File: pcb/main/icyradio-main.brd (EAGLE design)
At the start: 167.7 x 111.2 mm, 700 parts, among them CON101 FPC-22P, CON102 FPC-22P, CON1101 2EDG-2P-5MM-H, CON701 4P-SH-TOP, CON801 PCIE-X4-EDGE, J101 RJ45_MAG_LED_1G-TE-1-2301994-0, J701 TRSJACK, J702 TRSJACK, J703 TRSJACK, M701 SPH0641LM4H-1, M702 SPH0641LM4H-1, Q101 AO3400, Q102 AO3400, Q1101 AO3400, Q1102 AO4805, Q1103 AO3400, Q1104 AO4805, Q1105 AO4805, Q1106 AO3400, T501 UWB1-85E, T502 UWB1-85E, T503 UWB1-85E, T504 UWB1-85E, T505 UWB1-85E, T506 UWB1-85E, T507 UWB1-85E, T508 UWB1-85E, U1001 LTC4313-3, U1002 UPD301C, U1003 MIC2019, U101 MIC2019, U102 RPI-CM4, U1101 MCP1804-3302, U1102 LT7182S, U1201 ADM7172ACPZ-5.0, U1202 ADM7171ACPZ-1.3, U1203 ADM7171ACPZ-3.3, U1204 MIC23159, U1205 MIC5166, U1206 ADM7171ACPZ-1.3, U1207 ADM7171ACPZ-3.3, U1208 MIC23159, U1209 MIC23155, U1210 ADP7142AUJZ-3.3, U201 XC7A100TFGG484, U202 SST26VF064B, U301 MT41K256M16TW-125, U401 AD9361, U501 MIC2019, U502 MIC2019, U503 MIC2019, U504 MIC2019, U505 ADL5601, U506 ADL5601, U601 8V97003, U701 ADAU1372, U901 DSB321SDA, U902 SI5351C-B-GM

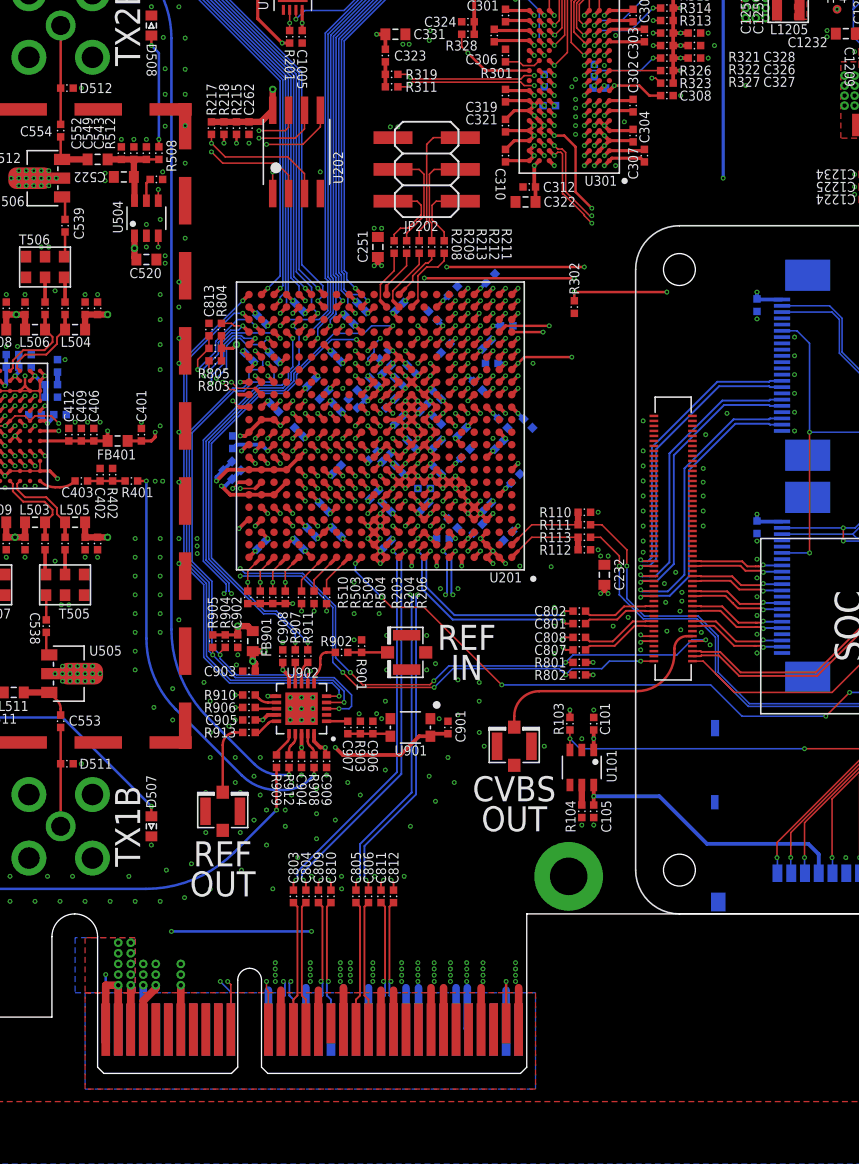
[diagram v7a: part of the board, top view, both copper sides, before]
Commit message: Some PCB rectifications and removal of old gerbers
Signed-off-by: João Silva <jgc3silva@gmail.com>
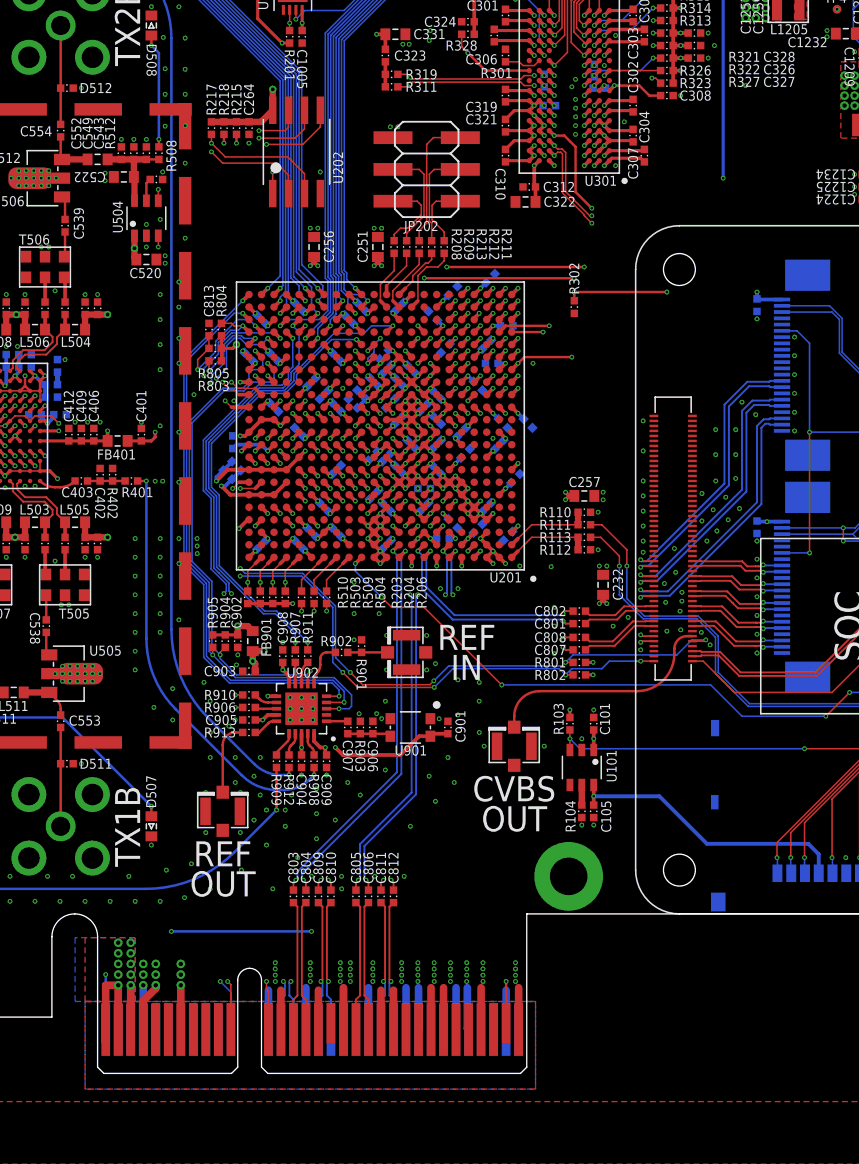
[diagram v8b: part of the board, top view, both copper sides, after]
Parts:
- added C263: 4.7uF, Capacitor:CAP0402
- added C264: 100nF, Capacitor:CAP0402
- C256: value 100nF -> 47uF; device Capacitor:CAP0402 -> Capacitor:CAP0603
- C257: value 4.7uF -> 47uF; device Capacitor:CAP0402 -> Capacitor:CAP0603
- C260: value 100nF -> 4.7uF
- C261: value 4.7uF -> 100nF
- moved C262 32.2 mm to (68.1, 32.5), flipped to the bottom, turned to 45 degrees
- moved C257 29.4 mm to (83.9, 33.4), flipped to the top, turned to 0 degrees
- moved C259 24.3 mm to (55.4, 35.1), turned to 45 degrees
- moved C256 22.6 mm to (62.3, 53.3), flipped to the top, turned to 90 degrees
- moved C260 13.1 mm to (79.4, 39.2), turned to 225 degrees
- moved C258 12.7 mm to (58.1, 47.5)
- moved C261 2.64 mm to (71.1, 32.5), turned to 315 degrees
- moved C232 0.81 mm to (85.4, 26.3)
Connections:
- net 1V0: now also C262.1, C263.1; no longer C260.1
- net 1V2: now also C257.1
- net 1V35: now also C260.1; no longer C259.1
- net 2V5: now also C259.1; no longer C258.1
- net 3V3: now also C258.1, C264.1; no longer C257.1, C262.1
- net GND: now also C263.2, C264.2
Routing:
- net CM4_CAM0_CSI_C_N: track 23.6 -> 22.1 mm
- net CM4_CAM0_CSI_C_P: track 23.6 -> 22.1 mm
- net CM4_CAM0_CSI_D1_P: track 23.4 -> 22.0 mm
- net CM4_CAM0_CSI_D0_N: track 23.2 -> 21.8 mm
- net CM4_CAM0_CSI_D1_N: track 23.4 -> 22.0 mm
- net CM4_CAM0_CSI_D0_P: track 23.2 -> 21.8 mm
- net 1V0: track 45.8 -> 47.0 mm, vias 47 -> 49
- net 1V2: track 17.3 -> 18.6 mm, vias 16 -> 18
- net 0V675_DDR3_VREF: track 155.2 -> 154.2 mm
- net 3V3_CM4: track 17.2 -> 16.6 mm
- net GND: vias 1475 -> 1490
